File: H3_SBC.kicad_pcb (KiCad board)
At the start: 6 copper layers, 50 x 40 mm, 14 parts, among them CN1 YXT-BB10-50P-02, CN2 YXT-BB10-50P-02, CN3 YXT-BB10-50P-02, Q1 WPM1481-6/TR, U1 H3, U10 XT28EG32GA4YJECGA, U2 AXP223_C2997893, U3 K4B4G1646E-BYMA 4GB, U4 K4B4G1646E-BYMA 4GB, U5 AP2127K-2.5, U9 RTL8211E-VB-CG, X1 X201232768KLD2SI, X2 SMD-5032_4P 24M 20pf, X3 5YAA25000121TF25E2

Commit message: linking symbols to footprints
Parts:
- added C1: 10uF, Capacitor_SMD:C_0603_1608Metric, F.Cu at (155.2, 65.5)
- added C10: 10uF, Capacitor_SMD:C_0603_1608Metric, F.Cu at (146.8, 63.3)
- added C100: 1uF, Capacitor_SMD:C_0402_1005Metric, F.Cu at (115.2, 69.6)
- added C101: 1uF, Capacitor_SMD:C_0402_1005Metric, F.Cu at (115.2, 71.5)
- added C102: 0.1uF, Capacitor_SMD:C_0603_1608Metric, F.Cu at (99.7, 78.5)
- added C103: 0.1uF, Capacitor_SMD:C_0603_1608Metric, F.Cu at (103.7, 65.9)
- added C104: 0.1uF, Capacitor_SMD:C_0603_1608Metric, F.Cu at (103.7, 68.4)
- added C105: 0.1uF, Capacitor_SMD:C_0603_1608Metric, F.Cu at (103.7, 70.9)
- added C106: 10uF, Capacitor_SMD:C_0603_1608Metric, F.Cu at (103.7, 73.4)
- added C107: 1uF, Capacitor_SMD:C_0402_1005Metric, F.Cu at (115.2, 73.5)
- added C108: 1uF, Capacitor_SMD:C_0402_1005Metric, F.Cu at (115.2, 75.5)
- added C109: 0.1uF, Capacitor_SMD:C_0603_1608Metric, F.Cu at (103.7, 75.9)
- added C11: 1uF, Capacitor_SMD:C_0402_1005Metric, F.Cu at (154.7, 58.0)
- added C110: 0.1uF, Capacitor_SMD:C_0603_1608Metric, F.Cu at (103.7, 78.5)
- added C111: 0.1uF, Capacitor_SMD:C_0603_1608Metric, F.Cu at (107.7, 65.9)
- added C112: 0.1uF, Capacitor_SMD:C_0603_1608Metric, F.Cu at (107.7, 68.4)
- added C113: 0.1uF, Capacitor_SMD:C_0603_1608Metric, F.Cu at (107.7, 70.9)
- added C114: 0.1uF, Capacitor_SMD:C_0603_1608Metric, F.Cu at (107.7, 73.4)
- added C115: 0.1uF, Capacitor_SMD:C_0603_1608Metric, F.Cu at (107.7, 75.9)
- added C116: 0.1uF, Capacitor_SMD:C_0603_1608Metric, F.Cu at (107.7, 78.5)
- added C117: 0.1uF, Capacitor_SMD:C_0603_1608Metric, F.Cu at (111.7, 65.9)
- added C118: 0.1uF, Capacitor_SMD:C_0603_1608Metric, F.Cu at (111.7, 68.4)
- added C119: 0.1uF, Capacitor_SMD:C_0603_1608Metric, F.Cu at (111.7, 70.9)
- added C12: 1uF, Capacitor_SMD:C_0402_1005Metric, F.Cu at (154.7, 60.0)
- added C120: 0.1uF, Capacitor_SMD:C_0603_1608Metric, F.Cu at (111.7, 73.4)
- added C121: 0.1uF, Capacitor_SMD:C_0603_1608Metric, F.Cu at (111.7, 75.9)
- added C122: 0.1uF, Capacitor_SMD:C_0603_1608Metric, B.Cu at (171.8, 67.5)
- added C123: 27pF, Capacitor_SMD:C_0402_1005Metric, F.Cu at (121.2, 91.7)
- added C124: 0.1uF, Capacitor_SMD:C_0603_1608Metric, F.Cu at (117.7, 97.0)
- added C125: 27pF, Capacitor_SMD:C_0402_1005Metric, F.Cu at (121.2, 93.7)
- added C126: 0.1uF, Capacitor_SMD:C_0603_1608Metric, F.Cu at (117.7, 99.5)
- added C127: 0.1uF, Capacitor_SMD:C_0603_1608Metric, F.Cu at (117.7, 102.0)
- added C128: 4.7uF, Capacitor_SMD:C_0603_1608Metric, F.Cu at (131.9, 62.0)
- added C129: 4.7uF, Capacitor_SMD:C_0603_1608Metric, F.Cu at (131.9, 64.5)
- added C13: 10uF, Capacitor_SMD:C_0603_1608Metric, F.Cu at (146.8, 65.8)
- added C130: 0.1uF, Capacitor_SMD:C_0603_1608Metric, F.Cu at (117.7, 104.5)
- added C14: 10uF, Capacitor_SMD:C_0603_1608Metric, F.Cu at (146.8, 68.3)
- added C15: 1uF, Capacitor_SMD:C_0402_1005Metric, F.Cu at (141.4, 58.0)
- added C16: 0.1uF, Capacitor_SMD:C_0603_1608Metric, F.Cu at (138.0, 58.3)
- added C17: 1uF, Capacitor_SMD:C_0402_1005Metric, F.Cu at (141.4, 60.0)
- added C18: 0.1uF, Capacitor_SMD:C_0603_1608Metric, F.Cu at (138.0, 60.8)
- added C19: 0.1uF, Capacitor_SMD:C_0603_1608Metric, F.Cu at (138.0, 63.3)
- added C2: 10uF, Capacitor_SMD:C_0603_1608Metric, F.Cu at (155.2, 67.2)
- added C20: 0.1uF, Capacitor_SMD:C_0603_1608Metric, F.Cu at (138.0, 65.8)
- added C21: 0.1uF, Capacitor_SMD:C_0603_1608Metric, F.Cu at (138.0, 68.3)
- added C22: 0.1uF, Capacitor_SMD:C_0603_1608Metric, F.Cu at (138.0, 70.8)
- added C23: 15pF, Capacitor_SMD:C_0402_1005Metric, B.Cu at (175.0, 67.5)
- added C24: 15pF, Capacitor_SMD:C_0402_1005Metric, F.Cu at (125.9, 68.8)
- added C25: 15pF, Capacitor_SMD:C_0402_1005Metric, F.Cu at (125.9, 70.8)
- added C26: 15pF, Capacitor_SMD:C_0402_1005Metric, F.Cu at (125.9, 72.8)
- added C27: 10uF, Capacitor_SMD:C_0603_1608Metric, F.Cu at (120.0, 58.1)
- added C28: 1nF, Capacitor_SMD:C_0805_2012Metric, F.Cu at (120.3, 55.4)
- added C29: 10uF, Capacitor_SMD:C_0603_1608Metric, F.Cu at (120.0, 60.6)
- added C3: 10uF, Capacitor_SMD:C_0603_1608Metric, F.Cu at (155.2, 69.0)
- added C30: 4.7uF, Capacitor_SMD:C_0603_1608Metric, F.Cu at (120.0, 63.1)
- added C31: 4.7uF, Capacitor_SMD:C_0603_1608Metric, F.Cu at (120.0, 65.7)
- added C32: 4.7uF, Capacitor_SMD:C_0603_1608Metric, F.Cu at (120.0, 68.2)
- added C33: 4.7uF, Capacitor_SMD:C_0603_1608Metric, F.Cu at (120.0, 70.7)
- added C34: 4.7uF, Capacitor_SMD:C_0603_1608Metric, F.Cu at (120.0, 73.2)
- added C35: 1uF, Capacitor_SMD:C_0402_1005Metric, F.Cu at (95.1, 97.8)
- added C36: 0.1uF, Capacitor_SMD:C_0603_1608Metric, F.Cu at (95.7, 83.0)
- added C37: 0.1uF, Capacitor_SMD:C_0603_1608Metric, F.Cu at (117.7, 92.0)
- added C38: 4.7uF, Capacitor_SMD:C_0603_1608Metric, F.Cu at (131.9, 57.0)
- added C39: 0.1uF, Capacitor_SMD:C_0603_1608Metric, F.Cu at (117.7, 94.5)
- added C4: 10uF, Capacitor_SMD:C_0603_1608Metric, F.Cu at (157.2, 66.0)
- added C40: 4.7uF, Capacitor_SMD:C_0603_1608Metric, F.Cu at (131.9, 59.5)
- added C41: 10uF, Capacitor_SMD:C_0603_1608Metric, F.Cu at (95.7, 85.5)
- added C42: 0.1uF, Capacitor_SMD:C_0603_1608Metric, F.Cu at (95.7, 88.0)
- added C43: 10uF, Capacitor_SMD:C_0603_1608Metric, F.Cu at (95.7, 90.5)
- added C44: 10uF, Capacitor_SMD:C_0603_1608Metric, F.Cu at (95.7, 93.0)
- added C45: 10uF, Capacitor_SMD:C_0603_1608Metric, F.Cu at (95.7, 95.5)
- added C46: 10uF, Capacitor_SMD:C_0603_1608Metric, F.Cu at (99.7, 83.0)
- added C47: 10uF, Capacitor_SMD:C_0603_1608Metric, F.Cu at (99.7, 85.5)
- added C48: 10uF, Capacitor_SMD:C_0603_1608Metric, F.Cu at (99.7, 88.0)
- added C49: 10uF, Capacitor_SMD:C_0603_1608Metric, F.Cu at (99.7, 90.5)
- added C5: 1nF, Capacitor_SMD:C_0805_2012Metric, F.Cu at (151.1, 58.5)
- added C50: 10uF, Capacitor_SMD:C_0603_1608Metric, F.Cu at (99.7, 93.0)
- added C51: 1uF, Capacitor_SMD:C_0402_1005Metric, F.Cu at (95.1, 99.7)
- added C52: 1uF, Capacitor_SMD:C_0402_1005Metric, F.Cu at (95.1, 101.7)
- added C53: 10uF, Capacitor_SMD:C_0603_1608Metric, F.Cu at (99.7, 95.5)
- added C54: 0.1uF, Capacitor_SMD:C_0603_1608Metric, F.Cu at (103.7, 83.0)
- added C55: 0.1uF, Capacitor_SMD:C_0603_1608Metric, F.Cu at (103.7, 85.5)
- added C56: 0.1uF, Capacitor_SMD:C_0603_1608Metric, F.Cu at (103.7, 88.0)
- added C57: 0.1uF, Capacitor_SMD:C_0603_1608Metric, F.Cu at (103.7, 90.5)
- added C58: 1uF, Capacitor_SMD:C_0402_1005Metric, F.Cu at (95.1, 103.7)
- added C59: 0.1uF, Capacitor_SMD:C_0603_1608Metric, F.Cu at (103.7, 93.0)
- added C6: 1nF, Capacitor_SMD:C_0805_2012Metric, F.Cu at (151.1, 61.6)
- added C60: 0.1uF, Capacitor_SMD:C_0603_1608Metric, F.Cu at (103.7, 95.5)
- added C61: 4.7uF, Capacitor_SMD:C_0603_1608Metric, F.Cu at (120.0, 75.7)
- added C62: 0.1uF, Capacitor_SMD:C_0603_1608Metric, F.Cu at (107.7, 83.0)
- added C63: 1uF, Capacitor_SMD:C_0402_1005Metric, F.Cu at (95.1, 105.6)
- added C64: 10uF, Capacitor_SMD:C_0603_1608Metric, F.Cu at (107.7, 85.5)
- added C65: 1nF, Capacitor_SMD:C_0805_2012Metric, F.Cu at (101.6, 98.3)
- added C66: 10uF, Capacitor_SMD:C_0603_1608Metric, F.Cu at (120.9, 83.0)
- added C67: 0.1uF, Capacitor_SMD:C_0603_1608Metric, F.Cu at (120.9, 85.5)
- added C68: 1uF, Capacitor_SMD:C_0402_1005Metric, F.Cu at (120.3, 87.7)
- added C69: 4.7uF, Capacitor_SMD:C_0603_1608Metric, F.Cu at (134.7, 69.0)
- added C7: 1nF, Capacitor_SMD:C_0805_2012Metric, F.Cu at (151.1, 64.6)
- added C70: 22uF, Capacitor_SMD:C_0805_2012Metric, F.Cu at (101.6, 101.3)
- added C71: 22uF, Capacitor_SMD:C_0805_2012Metric, F.Cu at (101.6, 104.3)
- added C72: 10uF, Capacitor_SMD:C_0603_1608Metric, F.Cu at (107.7, 88.0)
- added C73: 10uF, Capacitor_SMD:C_0603_1608Metric, F.Cu at (107.7, 90.5)
- added C74: 1uF, Capacitor_SMD:C_0402_1005Metric, F.Cu at (98.0, 97.8)
- added C75: 0.1uF, Capacitor_SMD:C_0603_1608Metric, F.Cu at (107.7, 93.0)
- added C76: 10uF, Capacitor_SMD:C_0603_1608Metric, F.Cu at (107.7, 95.5)
- added C77: 1uF, Capacitor_SMD:C_0402_1005Metric, F.Cu at (98.0, 99.7)
- added C78: 1uF, Capacitor_SMD:C_0402_1005Metric, F.Cu at (98.0, 101.7)
- added C79: 0.1uF, Capacitor_SMD:C_0603_1608Metric, F.Cu at (111.7, 83.0)
- added C8: 10uF, Capacitor_SMD:C_0603_1608Metric, F.Cu at (146.4, 58.0)
- added C80: 0.1uF, Capacitor_SMD:C_0603_1608Metric, F.Cu at (111.7, 85.5)
- added C81: 10uF, Capacitor_SMD:C_0603_1608Metric, F.Cu at (111.7, 88.0)
- added C82: 1uF, Capacitor_SMD:C_0402_1005Metric, F.Cu at (98.0, 103.7)
- added C83: 1uF, Capacitor_SMD:C_0402_1005Metric, F.Cu at (98.0, 105.6)
- added C84: 0.1uF, Capacitor_SMD:C_0603_1608Metric, F.Cu at (111.7, 90.5)
- added C85: 0.1uF, Capacitor_SMD:C_0603_1608Metric, F.Cu at (111.7, 93.0)
- added C86: 0.1uF, Capacitor_SMD:C_0603_1608Metric, F.Cu at (111.7, 95.5)
- added C87: 10uF, Capacitor_SMD:C_0603_1608Metric, F.Cu at (95.7, 65.9)
- added C88: 1uF, Capacitor_SMD:C_0402_1005Metric, F.Cu at (115.2, 65.6)
- added C89: 1uF, Capacitor_SMD:C_0402_1005Metric, F.Cu at (115.2, 67.6)
- added C9: 10uF, Capacitor_SMD:C_0603_1608Metric, F.Cu at (146.8, 60.8)
- added C90: 0.1uF, Capacitor_SMD:C_0603_1608Metric, F.Cu at (95.7, 68.4)
- added C91: 0.1uF, Capacitor_SMD:C_0603_1608Metric, F.Cu at (95.7, 70.9)
- added C92: 0.1uF, Capacitor_SMD:C_0603_1608Metric, F.Cu at (95.7, 73.4)
- added C93: 0.1uF, Capacitor_SMD:C_0603_1608Metric, F.Cu at (95.7, 75.9)
- added C94: 0.1uF, Capacitor_SMD:C_0603_1608Metric, F.Cu at (95.7, 78.5)
- added C95: 0.1uF, Capacitor_SMD:C_0603_1608Metric, F.Cu at (99.7, 65.9)
- added C96: 0.1uF, Capacitor_SMD:C_0603_1608Metric, F.Cu at (99.7, 68.4)
- added C97: 0.1uF, Capacitor_SMD:C_0603_1608Metric, F.Cu at (99.7, 70.9)
- added C98: 0.1uF, Capacitor_SMD:C_0603_1608Metric, F.Cu at (99.7, 73.4)
- added C99: 10uF, Capacitor_SMD:C_0603_1608Metric, F.Cu at (99.7, 75.9)
- added D1: RED, LED_SMD:LED_0402_1005Metric, F.Cu at (117.4, 82.7)
- added D2: YELLOW, LED_SMD:LED_0402_1005Metric, F.Cu at (117.4, 84.7)
- added D3: RED, LED_SMD:LED_0402_1005Metric, F.Cu at (117.4, 86.7)
- added L1: 1.5uH, Inductor_SMD:L_0402_1005Metric, F.Cu at (140.5, 85.1)
- added L2: 1.5uH, Inductor_SMD:L_0402_1005Metric, F.Cu at (140.5, 87.0)
- added L3: 1.5uH, Inductor_SMD:L_0402_1005Metric, F.Cu at (140.5, 89.0)
- added L4: 1.5uH, Inductor_SMD:L_0402_1005Metric, F.Cu at (140.5, 91.0)
- added L5: 2.2uH, Inductor_SMD:L_0402_1005Metric, F.Cu at (125.8, 85.1)
- added L6: 1.5uH, Inductor_SMD:L_0402_1005Metric, F.Cu at (140.5, 93.0)
- added L7: 1.5uH, Inductor_SMD:L_0402_1005Metric, F.Cu at (143.4, 85.1)
- added R1: 240R, Resistor_SMD:R_0402_1005Metric, F.Cu at (135.6, 85.1)
- added R10: 10mR, Resistor_SMD:R_0402_1005Metric, F.Cu at (143.4, 93.0)
- added R11: 2.2K, Resistor_SMD:R_0402_1005Metric, F.Cu at (146.3, 85.1)
- added R12: 2.2K, Resistor_SMD:R_0402_1005Metric, F.Cu at (146.3, 87.0)
- added R13: 51K, Resistor_SMD:R_0402_1005Metric, F.Cu at (146.3, 89.0)
- added R14: 47K, Resistor_SMD:R_0402_1005Metric, F.Cu at (130.7, 85.1)
- added R15: 100K, Resistor_SMD:R_0402_1005Metric, F.Cu at (130.7, 87.0)
- added R16: 330R, Resistor_SMD:R_0402_1005Metric, F.Cu at (130.7, 89.0)
- added R17: 330R, Resistor_SMD:R_0402_1005Metric, F.Cu at (130.7, 91.0)
- added R18: 330R, Resistor_SMD:R_0402_1005Metric, F.Cu at (130.7, 93.0)
- added R19: 220K, Resistor_SMD:R_0402_1005Metric, F.Cu at (130.7, 95.0)
- added R2: 240R, Resistor_SMD:R_0402_1005Metric, F.Cu at (135.6, 87.0)
- added R20: 2K, Resistor_SMD:R_0402_1005Metric, F.Cu at (135.6, 91.0)
- added R21: 2K, Resistor_SMD:R_0402_1005Metric, F.Cu at (135.6, 93.0)
- added R22: 100R, Resistor_SMD:R_0402_1005Metric, F.Cu at (135.6, 95.0)
- added R23: 20K, Resistor_SMD:R_0402_1005Metric, F.Cu at (125.8, 89.0)
- added R24: 4K7, Resistor_SMD:R_0402_1005Metric, F.Cu at (125.8, 91.0)
- added R25: 4K7, Resistor_SMD:R_0402_1005Metric, F.Cu at (125.8, 93.0)
- added R26: 4K7, Resistor_SMD:R_0402_1005Metric, F.Cu at (125.8, 95.0)
- added R27: 0R, Resistor_SMD:R_0402_1005Metric, F.Cu at (125.8, 97.0)
- added R3: 240R, Resistor_SMD:R_0402_1005Metric, F.Cu at (135.6, 89.0)
- added R4: 10K, Resistor_SMD:R_0402_1005Metric, F.Cu at (140.5, 97.0)
- added R5: 33R, Resistor_SMD:R_0402_1005Metric, F.Cu at (140.5, 99.0)
- added R6: 0, Resistor_SMD:R_0402_1005Metric, F.Cu at (143.4, 87.0)
- added R7: 2K49, Resistor_SMD:R_0402_1005Metric, F.Cu at (125.8, 87.0)
- added R8: 10mR, Resistor_SMD:R_0402_1005Metric, F.Cu at (143.4, 89.0)
- added R9: 10mR, Resistor_SMD:R_0402_1005Metric, F.Cu at (143.4, 91.0)
- moved U5 1.93 mm to (164.4, 66.6)
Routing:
- net GND: track 0.00 -> 0.92 mm

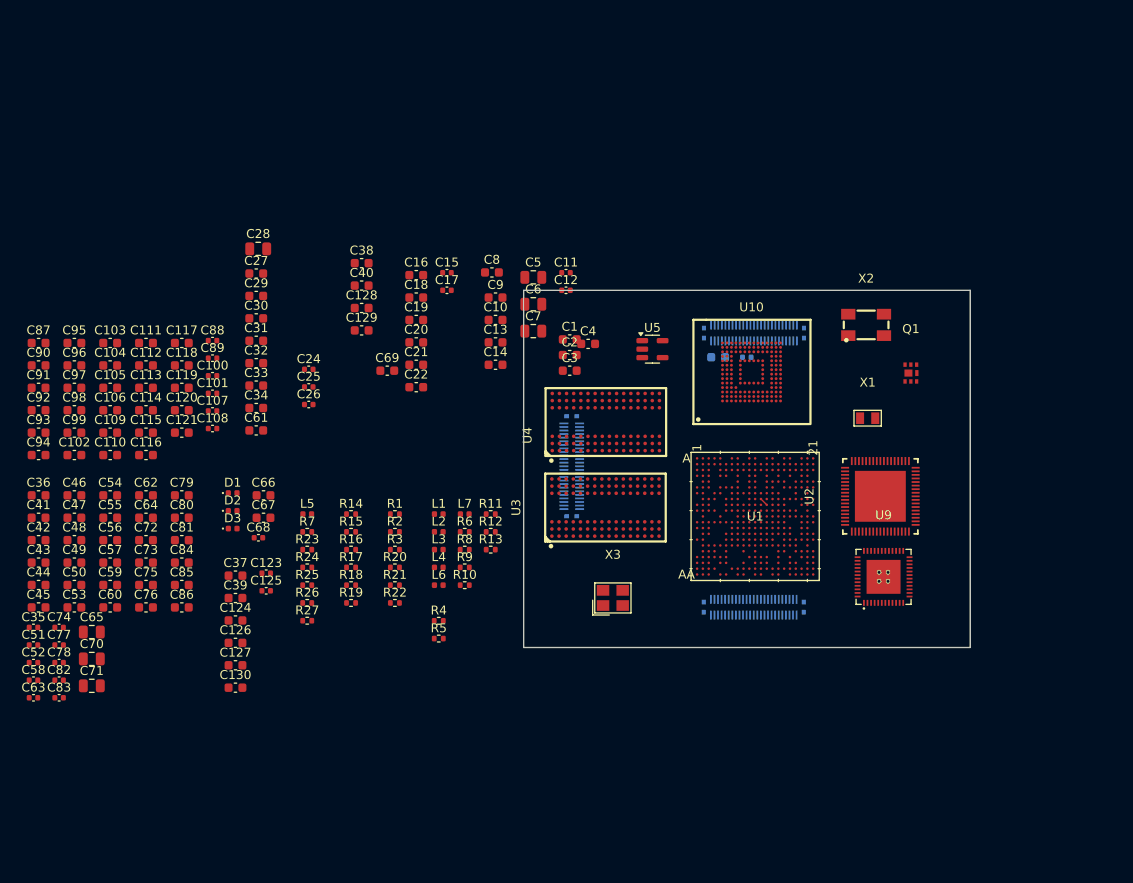
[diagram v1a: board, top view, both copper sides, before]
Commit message: placed major components
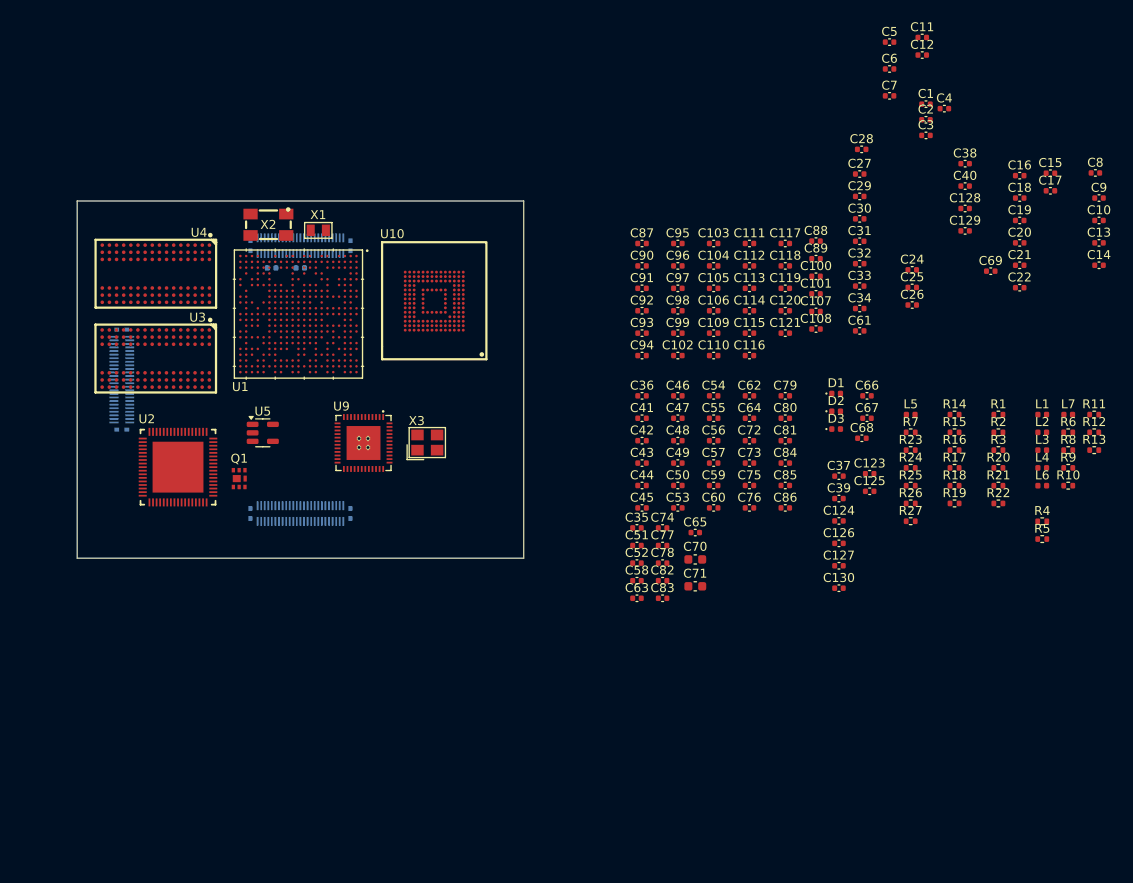
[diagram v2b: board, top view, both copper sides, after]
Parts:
- C1, C10, C102, C103, C104, C105, C106, C109, C110, C111, C112, C113, C114, C115, C116, C117, C118, C119, C120, C121, C122, C124, C126, C127, C128, C129, C13, C130, C14, C16, C18, C19, C2, C20, C21, C22, C27, C29, C3, C30, C31, C32, C33, C34, C36, C37, C38, C39, C4, C40, C41, C42, C43, C44, C45, C46, C47, C48, C49, C50, C53, C54, C55, C56, C57, C59, C60, C61, C62, C64, C66, C67, C69, C72, C73, C75, C76, C79, C8, C80, C81, C84, C85, C86, C87, C9, C90, C91, C92, C93, C94, C95, C96, C97, C98, C99: footprint Capacitor_SMD:C_0603_1608Metric -> Capacitor_SMD:C_0402_1005Metric
- C28, C5, C6, C65, C7: footprint Capacitor_SMD:C_0805_2012Metric -> Capacitor_SMD:C_0402_1005Metric
- C70, C71: footprint Capacitor_SMD:C_0805_2012Metric -> Capacitor_SMD:C_0603_1608Metric
- moved U2 78.7 mm to (111.3, 79.8), turned to 180 degrees
- moved Q1 76.1 mm to (118.1, 81.1)
- moved C103 68.5 mm to (171.3, 54.8)
- moved C104 68.5 mm to (171.3, 57.3)
- moved C105 68.5 mm to (171.3, 59.8)
- moved C106 68.5 mm to (171.3, 62.3)
- moved C109 68.5 mm to (171.3, 64.8)
- moved C110 68.5 mm to (171.3, 67.3)
- moved C128 68.5 mm to (199.4, 50.8)
- moved C129 68.5 mm to (199.4, 53.3)
- moved C38 68.5 mm to (199.4, 45.8)
- moved C40 68.5 mm to (199.4, 48.3)
- moved C54 68.5 mm to (171.3, 71.8)
- moved C55 68.5 mm to (171.3, 74.3)
- moved C56 68.5 mm to (171.3, 76.8)
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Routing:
- net GND: track 0.92 -> 0.00 mm

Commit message: placing capacitors
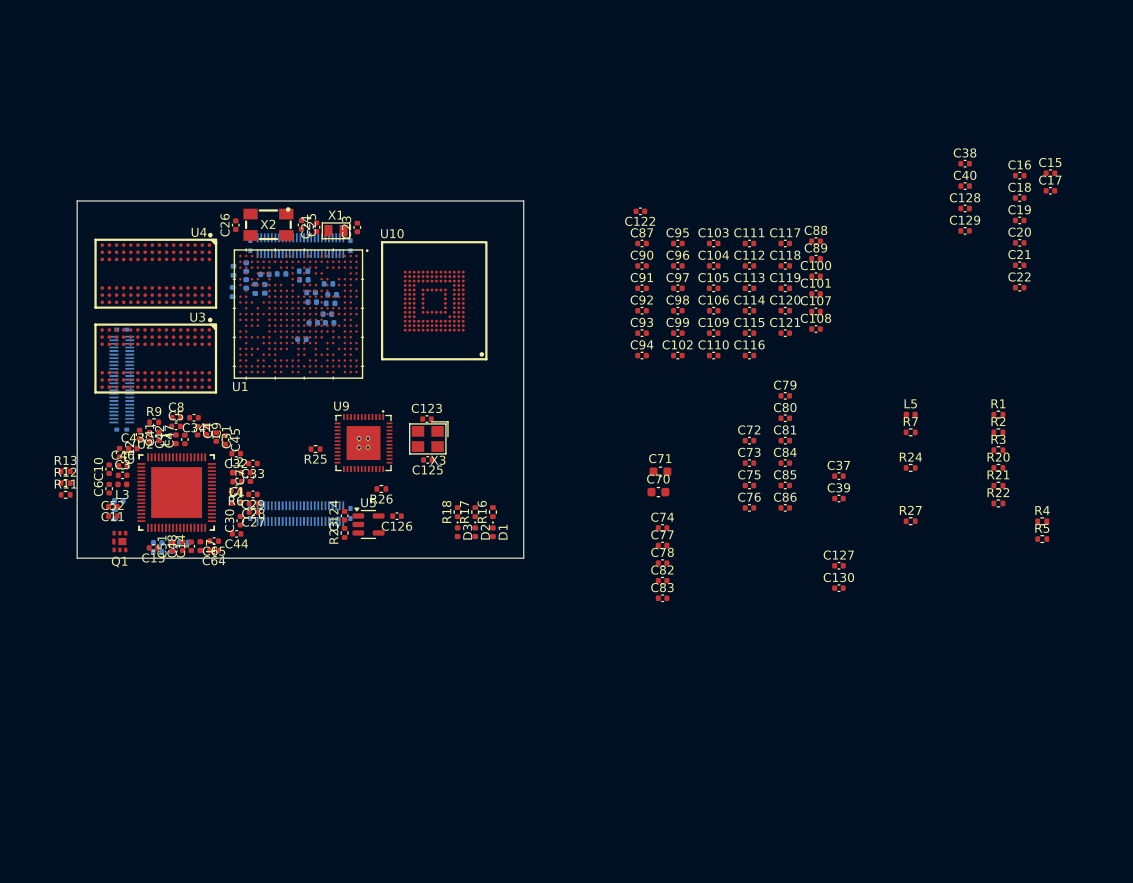
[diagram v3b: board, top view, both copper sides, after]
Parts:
- C122, C23: moved to F.Cu
- C35, C36, C49, C50, C53, C54, C55, C56, C57, C58, C59, C60, C61, C62, C63, C66, C67, C68, C69, L6, R10, R14, R15, R19, R8: moved to B.Cu
- moved R11 115.5 mm to (98.7, 82.9)
- moved R12 115.3 mm to (98.7, 81.6)
- moved R13 115.2 mm to (98.7, 80.3)
- moved C10 114.3 mm to (103.6, 80.0), turned to 90 degrees
- moved C13 111.3 mm to (108.5, 88.8), turned to 180 degrees
- moved R10 106.8 mm to (104.2, 85.1), turned to 90 degrees
- moved C8 106.5 mm to (111.1, 74.3)
- moved C14 106.4 mm to (112.8, 88.7), turned to 90 degrees
- moved C11 104.8 mm to (104.0, 84.2), turned to 180 degrees
- moved C9 103.3 mm to (114.5, 75.7), turned to -90 degrees
- moved L3 103.1 mm to (105.1, 81.7), turned to 180 degrees
- moved R9 102.5 mm to (108.6, 74.8)
- moved R8 101.0 mm to (110.5, 88.7), turned to -90 degrees
- moved C12 100.3 mm to (104.7, 78.2), turned to -90 degrees
- moved C6 99.2 mm to (103.6, 82.2), turned to 90 degrees
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
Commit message: moved some more capacitors
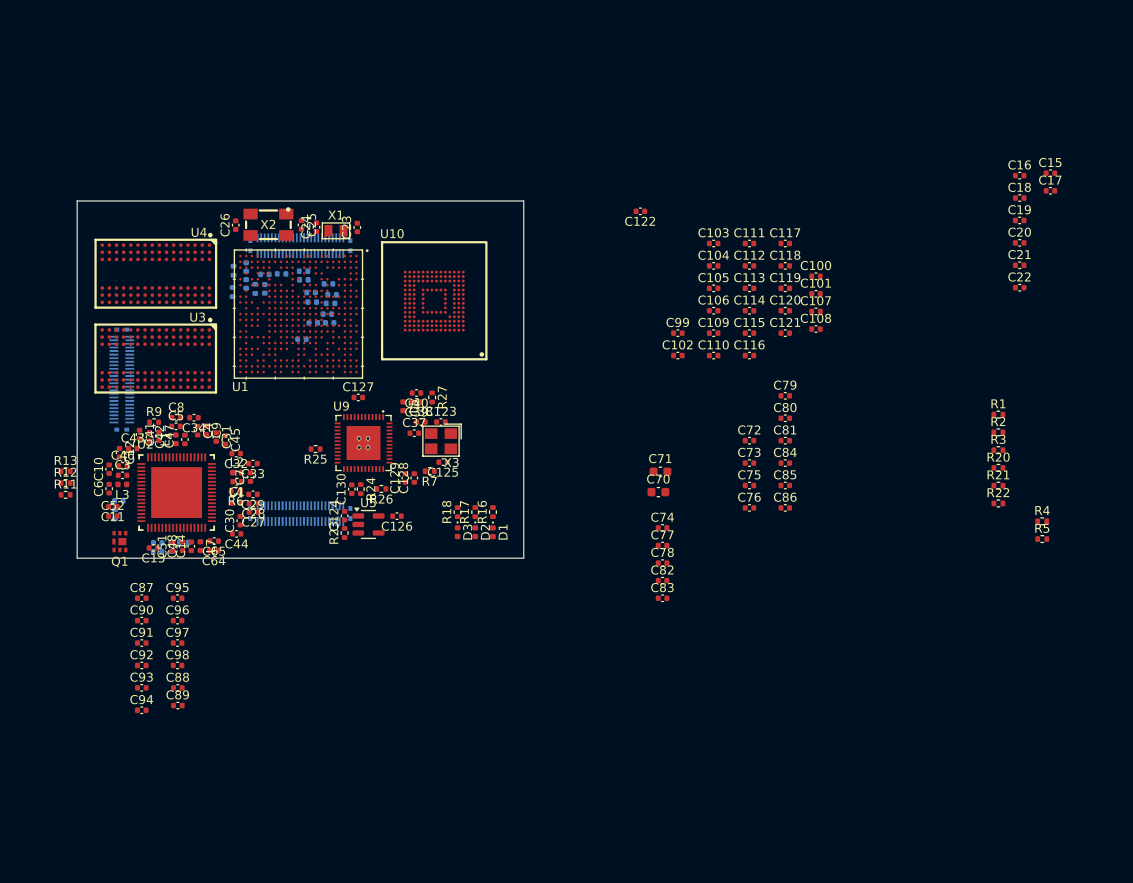
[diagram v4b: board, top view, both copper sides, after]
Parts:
- moved C88 87.2 mm to (111.3, 104.5)
- moved C89 87.2 mm to (111.3, 106.5)
- moved C87 68.7 mm to (107.2, 94.5)
- moved C91 68.7 mm to (107.2, 99.5)
- moved C92 68.7 mm to (107.2, 102.0)
- moved C95 68.7 mm to (111.2, 94.5)
- moved C97 68.7 mm to (111.2, 99.5)
- moved C98 68.7 mm to (111.2, 102.0)
- moved C90 68.7 mm to (107.2, 97.0)
- moved C93 68.7 mm to (107.2, 104.5)
- moved C94 68.7 mm to (107.2, 107.0)
- moved C96 68.7 mm to (111.2, 97.0)
- moved C128 68.7 mm to (137.8, 81.0), turned to 90 degrees
- moved C129 68.5 mm to (136.8, 81.0), turned to 90 degrees
- moved C38 67.5 mm to (138.5, 74.8)
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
